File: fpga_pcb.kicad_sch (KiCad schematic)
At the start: 0 parts

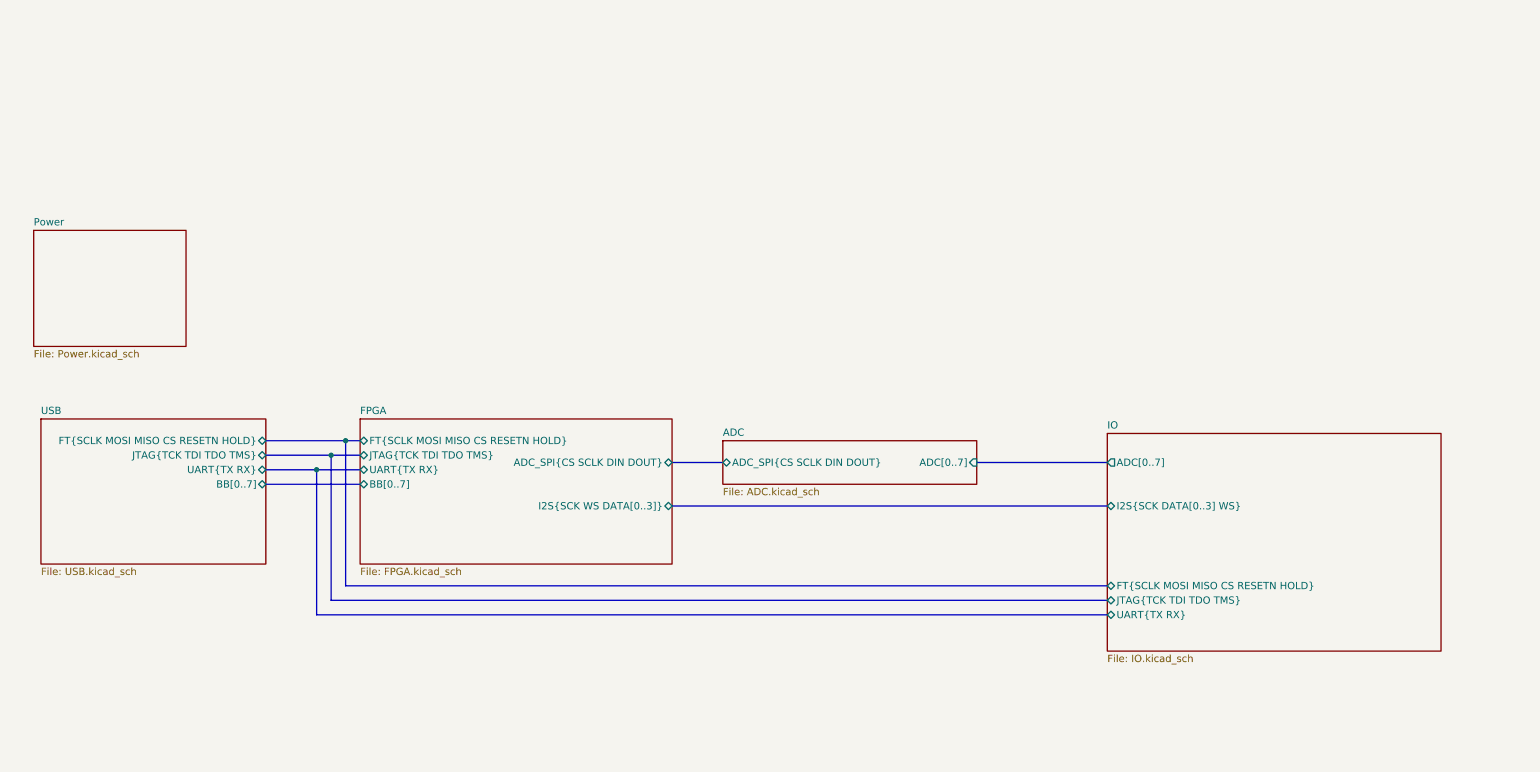
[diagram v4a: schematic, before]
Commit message: Added ethernet
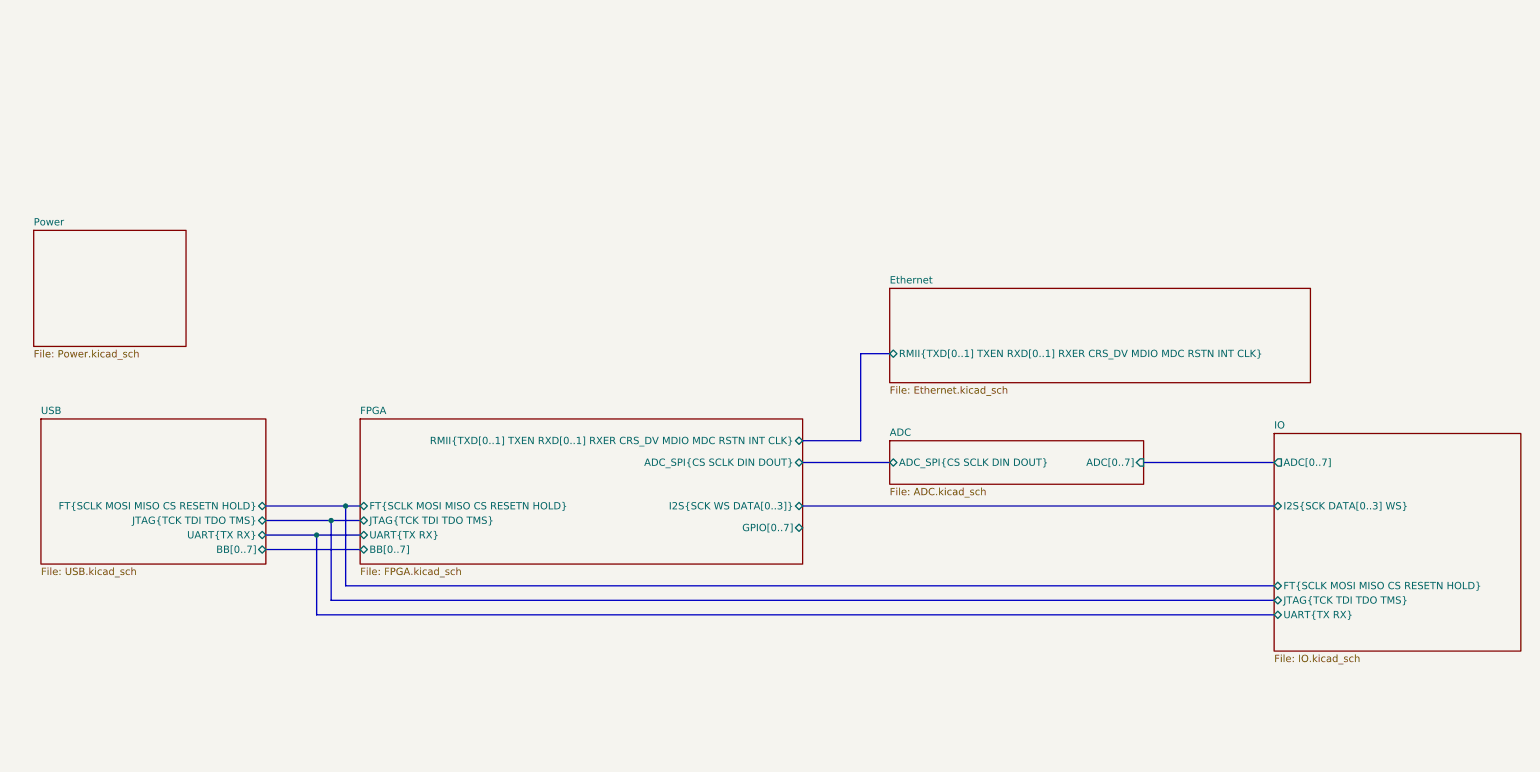
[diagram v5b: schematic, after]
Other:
- added sheet Ethernet (Ethernet.kicad_sch)
- sheet FPGA ports: added GPIO[0..7], RMII{TXD[0..1] TXEN RXD[0..1] RXER CRS_DV MDIO MDC RSTN INT CLK}; removed none

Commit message: Cleanup
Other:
- sheet IO ports: added GPIO[0..7]; removed none
- title: (none) -> FPGA PCB Top
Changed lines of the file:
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@@
 	(generator_version "10.0")
 	(paper "A4")
+	(title_block
+		(title "FPGA PCB Top")
+		(date "2026-09-19")
+	)
 	(junction
 		(at 72.39 104.14)
@@
 		(pts
 			(xy 214.63 93.98) (xy 237.49 93.98)
+		)
+		(stroke
+			(width 0)
+			(type default)
+		)
+	)
+	(bus
+		(pts
+			(xy 154.94 105.41) (xy 237.49 105.41)
 		)
 		(stroke
@@
 			(effects
 				(font
+					(size 1.27 1.27)
+				)
+				(justify left)
+			)
+		)
+		(pin "GPIO[0..7]" bidirectional
+			(at 237.49 105.41 180)
+			(effects
+				(font

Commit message: Started module-level layout
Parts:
- added H1, H2, H3, H4: MountingHole, MountingHole:MountingHole_3.2mm_M3_DIN965_Pad, symbol Mechanical:MountingHole
